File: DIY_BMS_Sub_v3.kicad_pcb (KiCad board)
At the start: 4 copper layers, 82 x 100 mm, 109 parts, among them J1 Conn_02x05_Top_Bottom, J2 Conn_02x05_Top_Bottom, J3 Conn_02x04_Top_Bottom, J4 Conn_02x04_Top_Bottom, J5 RJ45, Q1 Q_NMOS_GSD, Q2 Q_NMOS_GSD, Q3 Q_NMOS_GSD, Q4 Q_NMOS_GSD, Q5 Q_NMOS_GSD, Q6 Q_NMOS_GSD, SW1 SW_DIP_x04, U1 BQ76PL536A

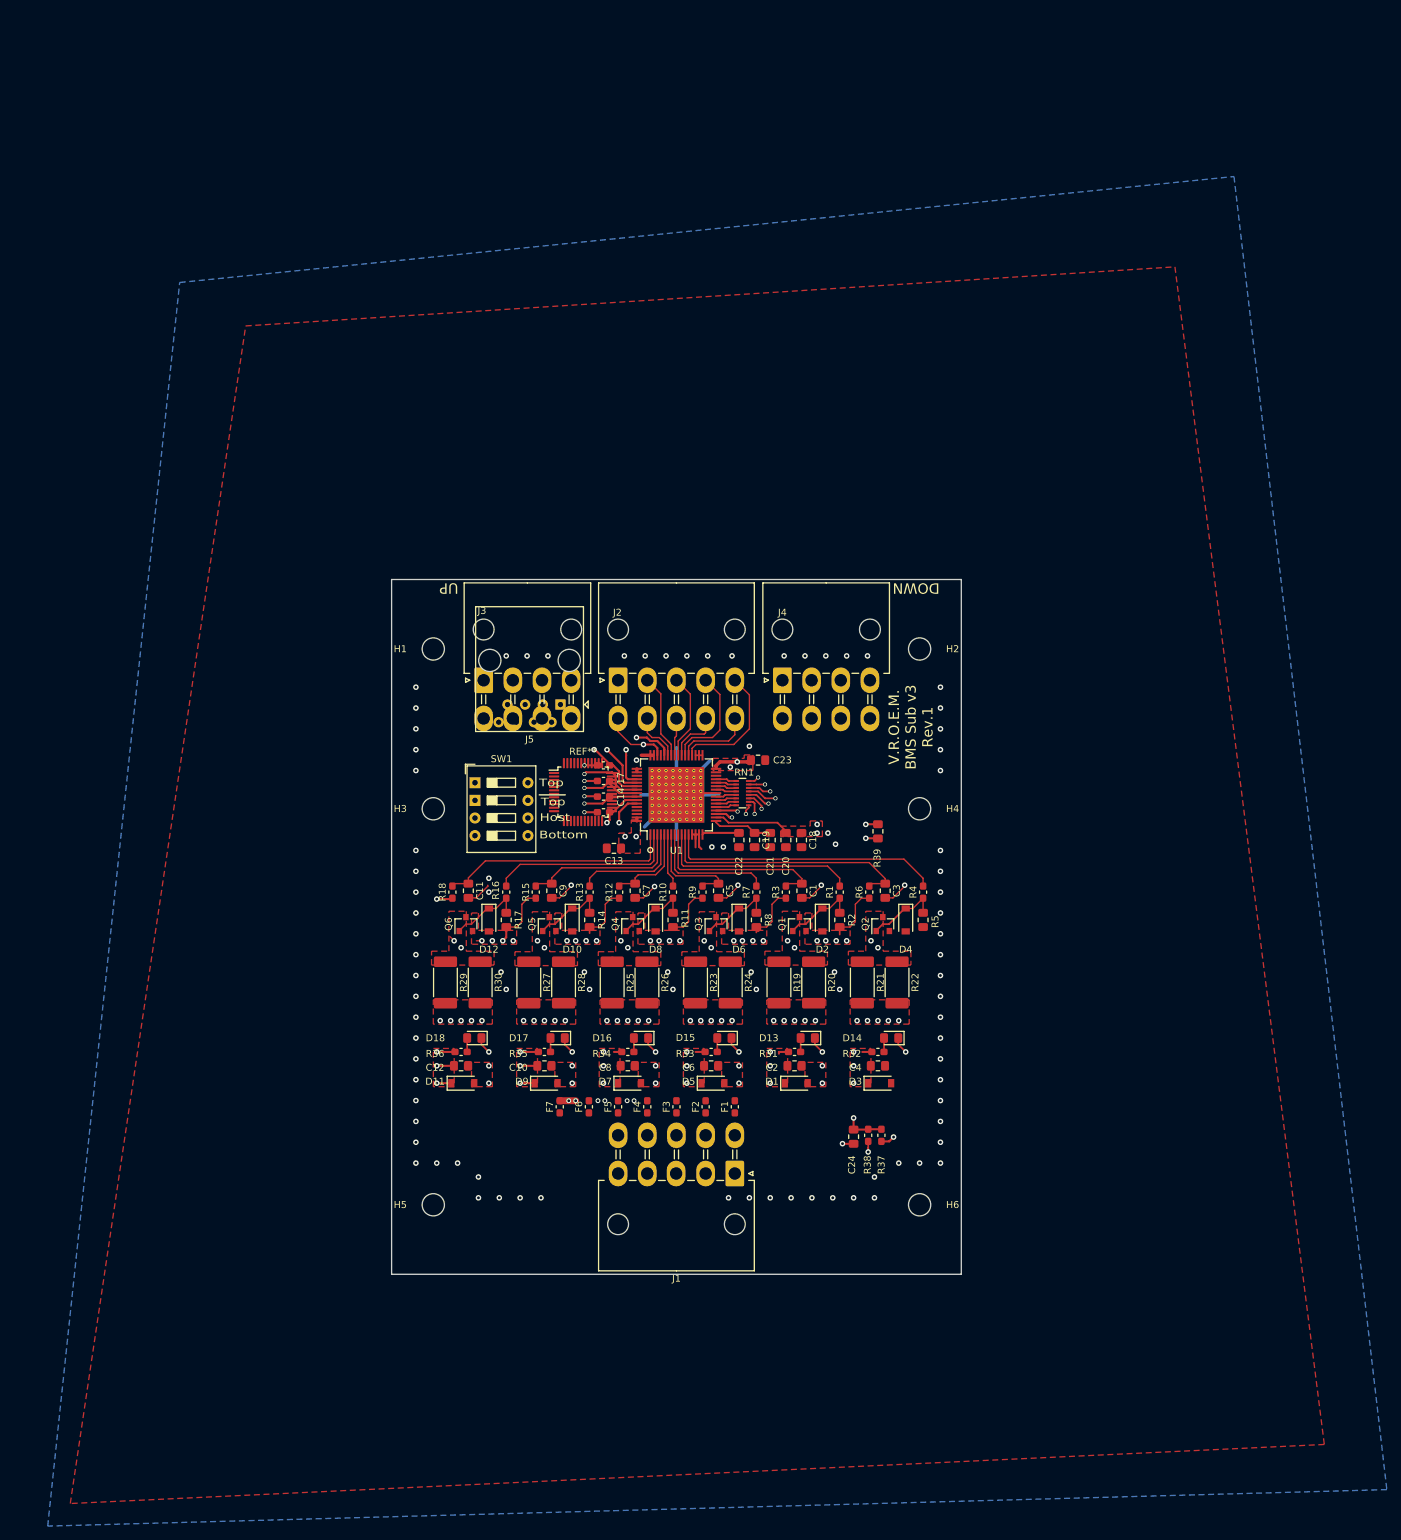
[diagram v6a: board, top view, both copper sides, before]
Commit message: Add files via upload
Changed board dimensions. Replaced Molex connectors from MiniFit to the smaller MicroFit-type.
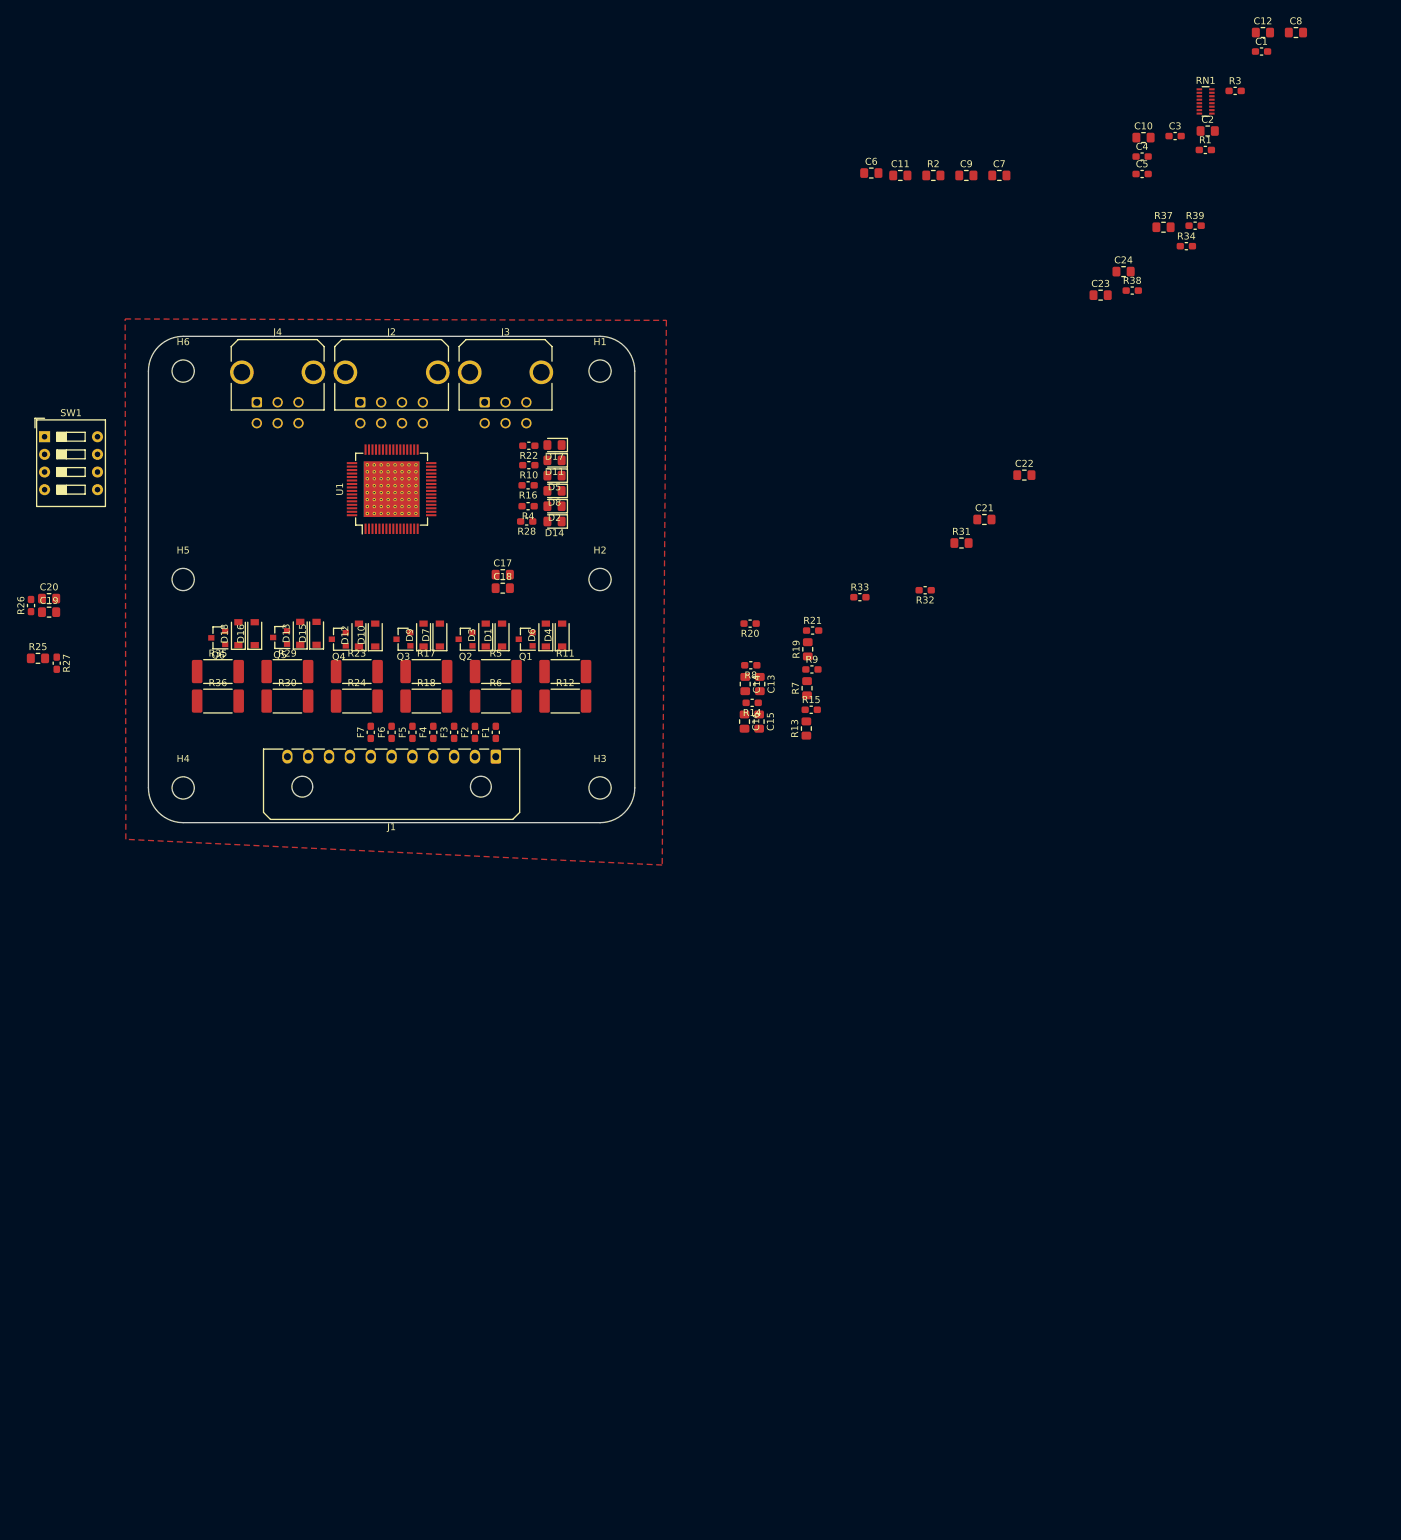
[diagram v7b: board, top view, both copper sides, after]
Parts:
- removed J5: RJ45, Connector_RJ:RJ45_Amphenol_54602-x08_Horizontal
- removed REF**: LQFP-48_7x7mm_P0.5mm, Package_QFP:LQFP-48_7x7mm_P0.5mm
- C1, C3, C4, C5: value 0.1u -> 33p; footprint Capacitor_SMD:C_0805_2012Metric_Pad1.15x1.40mm_HandSolder -> Capacitor_SMD:C_0603_1608Metric_Pad1.05x0.95mm_HandSolder
- C11, C7, C9: value 0.1u -> 2.2u
- C14, C15, C16, C17: value 33p -> 0.1u; footprint Capacitor_SMD:C_0603_1608Metric_Pad1.05x0.95mm_HandSolder -> Capacitor_SMD:C_0805_2012Metric_Pad1.15x1.40mm_HandSolder
- C20, C21, C23: value 2.2u -> 0.1u
- C22: value 10u -> 0.1u
- C24: value 47p -> 0.1u
- C6: value 0.1u -> 10u
- C8: value 0.1u -> 47p
- D11, D2, D5, D8: value 5V6 -> LED; footprint Diode_SMD:D_SOD-123 -> LED_SMD:LED_0805_2012Metric_Pad1.15x1.40mm_HandSolder
- D13, D15, D16, D18: value LED -> 5V6; footprint LED_SMD:LED_0805_2012Metric_Pad1.15x1.40mm_HandSolder -> Diode_SMD:D_SOD-123
- J1: value Conn_02x05_Top_Bottom -> Conn_01x11; footprint #_Connectors:Molex_Mini-Fit_Jr_5569-10A2_2x05_P4.20mm_Horizontal_with3d -> Connector_Molex:Molex_Micro-Fit_3.0_43650-1100_1x11_P3.00mm_Horizontal
- J2: value Conn_02x05_Top_Bottom -> Conn_02x04_Top_Bottom; footprint #_Connectors:Molex_Mini-Fit_Jr_5569-10A2_2x05_P4.20mm_Horizontal_with3d -> Connector_Molex:Molex_Micro-Fit_3.0_43045-0821_2x04-1MP_P3.00mm_Horizontal
- J3, J4: value Conn_02x04_Top_Bottom -> Conn_02x03_Top_Bottom; footprint #_Connectors:Molex_Mini-Fit_Jr_5569-08A2_2x04_P4.20mm_Horizontal_with3D -> Connector_Molex:Molex_Micro-Fit_3.0_43045-0621_2x03-1MP_P3.00mm_Horizontal
- R1: value 1K -> 1K82
- R10, R16, R4: value 1K -> 1k
- R11, R17, R5: value 1M -> 51; footprint Resistor_SMD:R_0805_2012Metric_Pad1.15x1.40mm_HandSolder -> Resistor_SMD:R_2512_6332Metric_Pad1.52x3.35mm_HandSolder
- R12, R18, R6: value 1K -> 51; footprint Resistor_SMD:R_0603_1608Metric_Pad1.05x0.95mm_HandSolder -> Resistor_SMD:R_2512_6332Metric_Pad1.52x3.35mm_HandSolder
- R13, R7: value 1K -> 1M; footprint Resistor_SMD:R_0603_1608Metric_Pad1.05x0.95mm_HandSolder -> Resistor_SMD:R_0805_2012Metric_Pad1.15x1.40mm_HandSolder
- R14, R8: value 1M -> 1K; footprint Resistor_SMD:R_0805_2012Metric_Pad1.15x1.40mm_HandSolder -> Resistor_SMD:R_0603_1608Metric_Pad1.05x0.95mm_HandSolder
- R19, R25: value 51 -> 1M; footprint Resistor_SMD:R_2512_6332Metric_Pad1.52x3.35mm_HandSolder -> Resistor_SMD:R_0805_2012Metric_Pad1.15x1.40mm_HandSolder
- R2: value 1M -> 100K
- R20, R21, R26, R27: value 51 -> 1K; footprint Resistor_SMD:R_2512_6332Metric_Pad1.52x3.35mm_HandSolder -> Resistor_SMD:R_0603_1608Metric_Pad1.05x0.95mm_HandSolder
- R22, R28: value 51 -> 1k; footprint Resistor_SMD:R_2512_6332Metric_Pad1.52x3.35mm_HandSolder -> Resistor_SMD:R_0603_1608Metric_Pad1.05x0.95mm_HandSolder
- R3: value 1K -> 1K47
- R31: value 1k -> 1M; footprint Resistor_SMD:R_0603_1608Metric_Pad1.05x0.95mm_HandSolder -> Resistor_SMD:R_0805_2012Metric_Pad1.15x1.40mm_HandSolder
- R32, R33: value 1k -> 1K
- R35, R36: value 1k -> 51; footprint Resistor_SMD:R_0603_1608Metric_Pad1.05x0.95mm_HandSolder -> Resistor_SMD:R_2512_6332Metric_Pad1.52x3.35mm_HandSolder
- R37: value 1K47 -> 1M; footprint Resistor_SMD:R_0603_1608Metric_Pad1.05x0.95mm_HandSolder -> Resistor_SMD:R_0805_2012Metric_Pad1.15x1.40mm_HandSolder
- R38: value 1K82 -> 1K
- R39: value 100K -> 1K; footprint Resistor_SMD:R_0805_2012Metric_Pad1.15x1.40mm_HandSolder -> Resistor_SMD:R_0603_1608Metric_Pad1.05x0.95mm_HandSolder
- moved C12 188.3 mm to (125.4, -78.7)
- moved C8 177.1 mm to (130.2, -78.7)
- moved H6 160.1 mm to (-30.0, -30.0)
- moved C10 159.0 mm to (108.2, -63.6)
- moved C2 147.1 mm to (117.5, -64.6)
- moved R34 141.1 mm to (114.4, -48.0), turned to 0 degrees
- moved C1 137.7 mm to (125.2, -76.0), turned to 0 degrees
- moved R37 136.9 mm to (111.1, -50.7), turned to 0 degrees
- moved C4 136.3 mm to (108.0, -60.9)
- moved R3 132.2 mm to (121.4, -70.3), turned to 0 degrees
- moved C6 130.6 mm to (69.0, -58.5)
- moved C24 130.4 mm to (105.4, -44.3), turned to 0 degrees
- moved R38 127.4 mm to (106.6, -41.6), turned to 0 degrees
- moved C11 120.3 mm to (73.2, -58.2), turned to 0 degrees
- moved C5 119.8 mm to (108.0, -58.4), turned to 0 degrees
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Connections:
- C1 pad 1: /S2_components/VC+ -> SW_NotTop
- C1 pad 2: AGND -> SDO_N
- C10 pad 1: /C5 -> Net-(C10-Pad1)
- C10 pad 2: /C4 -> AGND
- C11 pad 1: /S6_components/VC+ -> AGND
- C11 pad 2: AGND -> LDOD
- C12 pad 1: /C6 -> LDOD
- C12 pad 2: /C5 -> AGND
- C13 pad 1: AGND -> /C2
- C13 pad 2: /C6 -> /C1
- C14 pad 1: SW_NotTop -> /S2_components/VC+
- C14 pad 2: DRDY_N -> AGND
- C15 pad 1: SW_NotTop -> /C1
- C15 pad 2: ALERT_N -> AGND
- C16 pad 1: SW_NotTop -> /S1_components/VC+
- C16 pad 2: FAULT_N -> AGND
- C17 pad 1: SW_NotTop -> S3
- C17 pad 2: SDO_N -> /C2
- C18 pad 1: LDOD -> /S3_components/VC+
- C19 pad 1: Net-(C19-Pad1) -> /C4
- C19 pad 2: AGND -> S3
- C2 pad 1: /C2 -> AGND
- C2 pad 2: /C1 -> /C6
- C20 pad 1: AGND -> /S4_components/VC+
- C20 pad 2: LDOD -> AGND
- C21 pad 1: AGND -> /C5
- C21 pad 2: Net-(C19-Pad1) -> /C4
- C22 pad 1: AGND -> /S5_components/VC+
- C22 pad 2: Net-(C22-Pad2) -> AGND
- C23 pad 1: 5VDC -> /C6
- C23 pad 2: AGND -> /C5
- C24 pad 1: Net-(C24-Pad1) -> /S6_components/VC+
- C24 pad 2: 5VDC -> AGND
- C3 pad 1: /S1_components/VC+ -> SW_NotTop
- C3 pad 2: AGND -> FAULT_N
- C4 pad 1: /C1 -> SW_NotTop
- C4 pad 2: AGND -> ALERT_N
- C5 pad 1: /S3_components/VC+ -> SW_NotTop
- C5 pad 2: AGND -> DRDY_N
- C6 pad 1: S3 -> AGND
- C6 pad 2: /C2 -> Net-(C6-Pad2)
- C7 pad 1: /S4_components/VC+ -> 5VDC
- C8 pad 1: /C4 -> Net-(C8-Pad1)
- C8 pad 2: S3 -> 5VDC
- C9 pad 1: /S5_components/VC+ -> AGND
- C9 pad 2: AGND -> Net-(C10-Pad1)
- D10 pad 1: Net-(D10-Pad1) -> /C4
- D10 pad 2: /C4 -> S3
- D11 pad 1: /C6 -> Net-(D11-Pad1)
- D11 pad 2: /C5 -> Net-(D11-Pad2)
- D12 pad 2: /C5 -> S3
- D13 pad 1: Net-(D13-Pad1) -> /C5
- D13 pad 2: Net-(D13-Pad2) -> /C4
- D15 pad 2: Net-(D15-Pad2) -> /C4
- D16 pad 1: Net-(D16-Pad1) -> /C6
- D16 pad 2: Net-(D16-Pad2) -> /C5
- D18 pad 2: Net-(D18-Pad2) -> /C5
- D2 pad 2: /C1 -> Net-(D2-Pad2)
- D3 pad 1: /C1 -> Net-(D3-Pad1)
- D3 pad 2: AGND -> /C1
- D4 pad 1: Net-(D4-Pad1) -> /C1
- D5 pad 1: S3 -> Net-(D5-Pad1)
- D5 pad 2: /C2 -> Net-(D5-Pad2)
- D6 pad 2: /C2 -> AGND
- D7 pad 1: /C4 -> S3
- D7 pad 2: S3 -> /C2
- D8 pad 2: S3 -> Net-(D8-Pad2)
- D9 pad 1: /C5 -> Net-(D9-Pad1)
- D9 pad 2: /C4 -> /C2
- F4 pad 1: C3 -> (no net)
- J1 pad 1: 5VDC -> S0
- J1 pad 10: S4 -> (no net)
- J1 pad 2: Temp- -> S1
- J1 pad 3: (no net) -> S2
- J1 pad 4: S6 -> S3
- J1 pad 5: S5 -> S4
- J1 pad 6: S0 -> S5
- J1 pad 7: S1 -> S6
- J1 pad 8: S2 -> (no net)
- J1 pad 9: C3 -> (no net)
- J2 pad 1: AGND -> (no net)
- J2 pad 2: SDI_H -> (no net)
- J2 pad 3: SCLK_H -> (no net)
- J2 pad 4: ALERT_H -> (no net)
- J2 pad 5: CONV_H -> (no net)
- J2 pad 6: LDOD -> (no net)
- J2 pad 7: CS_H -> (no net)
- J2 pad 8: SDO_H -> (no net)
- J3 pad 2: FAULT_N -> SDO_N
- J3 pad 3: SDO_N -> CS_N
- J3 pad 4: CS_N -> CONV_N
- J3 pad 5: CONV_N -> SCLK_N
- J3 pad 6: ALERT_N -> SDI_N
- J4 pad 1: SDI_S -> DRDY_S
- J4 pad 2: SCLK_S -> (no net)
- J4 pad 3: ALERT_S -> CS_S
- J4 pad 5: CS_S -> SCLK_S
- J4 pad 6: SDO_S -> (no net)
- Q1 pad 1: Net-(D2-Pad1) -> Net-(D6-Pad1)
- Q1 pad 2: /C1 -> AGND
- Q1 pad 3: Net-(D13-Pad1) -> Net-(D5-Pad1)
- Q2 pad 1: Net-(D4-Pad1) -> Net-(D3-Pad1)
- Q2 pad 2: AGND -> /C1
- Q2 pad 3: Net-(D14-Pad1) -> Net-(D2-Pad1)
- Q3 pad 1: Net-(D6-Pad1) -> Net-(D9-Pad1)
- Q3 pad 3: Net-(D15-Pad1) -> Net-(D8-Pad1)
- Q4 pad 1: Net-(D8-Pad1) -> Net-(D12-Pad1)
- Q4 pad 3: Net-(D16-Pad1) -> Net-(D11-Pad1)
- Q5 pad 1: Net-(D10-Pad1) -> Net-(D15-Pad1)
- Q5 pad 3: Net-(D17-Pad1) -> Net-(D14-Pad1)
- Q6 pad 1: Net-(D12-Pad1) -> Net-(D18-Pad1)
- Q6 pad 3: Net-(D18-Pad1) -> Net-(D17-Pad1)
- R1 pad 1: Net-(D2-Pad1) -> Net-(R1-Pad1)
- R1 pad 2: /S2_components/Balancing -> Net-(C8-Pad1)
- R10 pad 1: Net-(D8-Pad1) -> Net-(D5-Pad2)
- R10 pad 2: /S4_components/Balancing -> /C1
- R11 pad 1: S3 -> Net-(D5-Pad1)
- R11 pad 2: Net-(D8-Pad1) -> /C1
- R12 pad 1: /C4 -> Net-(D5-Pad1)
- R12 pad 2: /S4_components/VC+ -> /C1
- R13 pad 1: Net-(D10-Pad1) -> AGND
- R13 pad 2: /S5_components/Balancing -> Net-(D6-Pad1)
- R14 pad 1: /C4 -> /C1
- R14 pad 2: Net-(D10-Pad1) -> /S1_components/VC+
- R15 pad 1: /C5 -> Net-(D6-Pad1)
- R15 pad 2: /S5_components/VC+ -> /S1_components/Balancing
- R16 pad 1: Net-(D12-Pad1) -> Net-(D8-Pad2)
- R16 pad 2: /S6_components/Balancing -> S3
- R17 pad 1: /C5 -> Net-(D8-Pad1)
- R17 pad 2: Net-(D12-Pad1) -> S3
- R18 pad 1: /C6 -> Net-(D8-Pad1)
- R18 pad 2: /S6_components/VC+ -> S3
- R19 pad 1: Net-(D13-Pad1) -> /C2
- R19 pad 2: /C2 -> Net-(D9-Pad1)
- R2 pad 1: /C1 -> 5VDC
- R2 pad 2: Net-(D2-Pad1) -> SW_Host
- R20 pad 1: Net-(D13-Pad1) -> S3
- R20 pad 2: /C2 -> /S3_components/VC+
- R21 pad 1: Net-(D14-Pad1) -> Net-(D9-Pad1)
- R21 pad 2: /C1 -> /S3_components/Balancing
- R22 pad 1: Net-(D14-Pad1) -> Net-(D11-Pad2)
- R22 pad 2: /C1 -> /C4
- R23 pad 1: Net-(D15-Pad1) -> Net-(D11-Pad1)
- R23 pad 2: S3 -> /C4
- R24 pad 1: Net-(D15-Pad1) -> Net-(D11-Pad1)
- R24 pad 2: S3 -> /C4
- R25 pad 1: Net-(D16-Pad1) -> S3
- R25 pad 2: /C4 -> Net-(D12-Pad1)
- R26 pad 1: Net-(D16-Pad1) -> /C4
- R26 pad 2: /C4 -> /S4_components/VC+
- R27 pad 1: Net-(D17-Pad1) -> Net-(D12-Pad1)
- R27 pad 2: /C5 -> /S4_components/Balancing
- R28 pad 1: Net-(D17-Pad1) -> Net-(D14-Pad2)
- R29 pad 1: Net-(D18-Pad1) -> Net-(D14-Pad1)
- R29 pad 2: /C6 -> /C5
- R3 pad 1: /C2 -> Net-(C8-Pad1)
- R3 pad 2: /S2_components/VC+ -> (no net)
- R30 pad 1: Net-(D18-Pad1) -> Net-(D14-Pad1)
- R30 pad 2: /C6 -> /C5
- R31 pad 1: Net-(D13-Pad2) -> /C4
- R31 pad 2: /C2 -> Net-(D15-Pad1)
- R32 pad 1: Net-(D14-Pad2) -> /C5
- R32 pad 2: /C1 -> /S5_components/VC+
- R33 pad 1: Net-(D15-Pad2) -> Net-(D15-Pad1)
- R33 pad 2: S3 -> /S5_components/Balancing
- R34 pad 1: Net-(D16-Pad2) -> Net-(D17-Pad2)
- R34 pad 2: /C4 -> /C6
- R35 pad 1: Net-(D17-Pad2) -> Net-(D17-Pad1)
- R35 pad 2: /C5 -> /C6
- R36 pad 1: Net-(D18-Pad2) -> Net-(D17-Pad1)
- R37 pad 1: Net-(C24-Pad1) -> /C5
- R37 pad 2: Temp- -> Net-(D18-Pad1)
- R38 pad 1: Net-(R38-Pad1) -> /C6
- R38 pad 2: Net-(C24-Pad1) -> /S6_components/VC+
- R39 pad 1: 5VDC -> Net-(D18-Pad1)
- R39 pad 2: SW_Host -> /S6_components/Balancing
- R4 pad 1: Net-(D4-Pad1) -> Net-(D2-Pad2)
- R4 pad 2: /S1_components/Balancing -> /C2
- R5 pad 1: AGND -> Net-(D2-Pad1)
- R5 pad 2: Net-(D4-Pad1) -> /C2
- R6 pad 1: /C1 -> Net-(D2-Pad1)
- R6 pad 2: /S1_components/VC+ -> /C2
- R7 pad 1: Net-(D6-Pad1) -> /C1
- R7 pad 2: /S3_components/Balancing -> Net-(D3-Pad1)
- R8 pad 2: Net-(D6-Pad1) -> /S2_components/VC+
- R9 pad 1: S3 -> Net-(D3-Pad1)
- R9 pad 2: /S3_components/VC+ -> /S2_components/Balancing
- RN1 pad 3: ALERT_S -> (no net)
- RN1 pad 4: FAULT_S -> (no net)
- RN1 pad 6: SDO_S -> (no net)
- RN1 pad 7: SDI_S -> (no net)
- U1 pad 16: Net-(C22-Pad2) -> Net-(C6-Pad2)
- U1 pad 17: Net-(C19-Pad1) -> Net-(C10-Pad1)
- U1 pad 19: Net-(R38-Pad1) -> Net-(R1-Pad1)
- U1 pad 20: Net-(C24-Pad1) -> Net-(C8-Pad1)
- U1 pad 36: CONV_H -> (no net)
- U1 pad 37: DRDY_H -> (no net)
- U1 pad 38: ALERT_H -> (no net)
- U1 pad 39: FAULT_H -> (no net)
- U1 pad 40: SCLK_H -> (no net)
- U1 pad 41: SDO_H -> (no net)
- U1 pad 42: SDI_H -> (no net)
- U1 pad 43: CS_H -> (no net)
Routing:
- net S6: track 102.6 -> 0.00 mm, vias 11 -> 0
- net 5VDC: track 99.1 -> 0.00 mm, vias 4 -> 0
- net Net-(C24-Pad1): track 86.4 -> 0.00 mm, vias 3 -> 0
- net Net-(R38-Pad1): track 85.5 -> 0.00 mm, vias 3 -> 0
- net CONV_S: track 79.1 -> 0.00 mm, vias 1 -> 0
- net AGND: track 74.0 -> 0.00 mm, vias 95 -> 0
- net SW_Host: track 73.2 -> 0.00 mm, vias 2 -> 0
- net /C5: track 60.8 -> 0.00 mm, vias 14 -> 0
- net LDOD: track 58.6 -> 0.00 mm, vias 3 -> 0
- net S3: track 53.2 -> 0.00 mm, vias 14 -> 0
- net S1: track 48.7 -> 0.00 mm, vias 14 -> 0
- net S2: track 47.2 -> 0.00 mm, vias 14 -> 0
- net S4: track 46.2 -> 0.00 mm, vias 14 -> 0
- net SW_NotTop: track 42.8 -> 0.00 mm, vias 4 -> 0
- net /S1_components/Balancing: track 39.4 -> 0.00 mm
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- removed copper zone on F.Cu, net /C5
- removed copper zone on F.Cu, net 5VDC
- removed copper zone on B.Cu, net AGND
- removed copper zone on F.Cu, net LDOD
- removed copper zone on F.Cu, net Net-(D13-Pad1)
- removed copper zone on F.Cu, net Net-(D14-Pad1)
- removed copper zone on F.Cu, net Net-(D15-Pad1)
- removed copper zone on F.Cu, net Net-(D16-Pad1)
- removed copper zone on F.Cu, net Net-(D17-Pad1)
- removed copper zone on F.Cu, net Net-(D18-Pad1)
- removed copper zone on F.Cu, net S1
- removed copper zone on F.Cu, net S2
- removed copper zone on F.Cu, net S3
- removed copper zone on F.Cu, net S4
- removed copper zone on F.Cu, net S5
- removed copper zone on F.Cu, net S6
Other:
- board size 82 x 100 mm -> 70 x 70 mm
- board text removed: "Bottom"
- board text removed: "C14-17"
- board text removed: "DOWN"
- board text removed: "Host"
- board text removed: "JLCJLCJLCJLC"
- board text removed: "Top"
- board text removed: "UP"
- board text removed: "V.R.O.E.M. BMS Sub v3 Rev.1"

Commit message: Add files via upload
Placed most components. Started routing and placing vias.
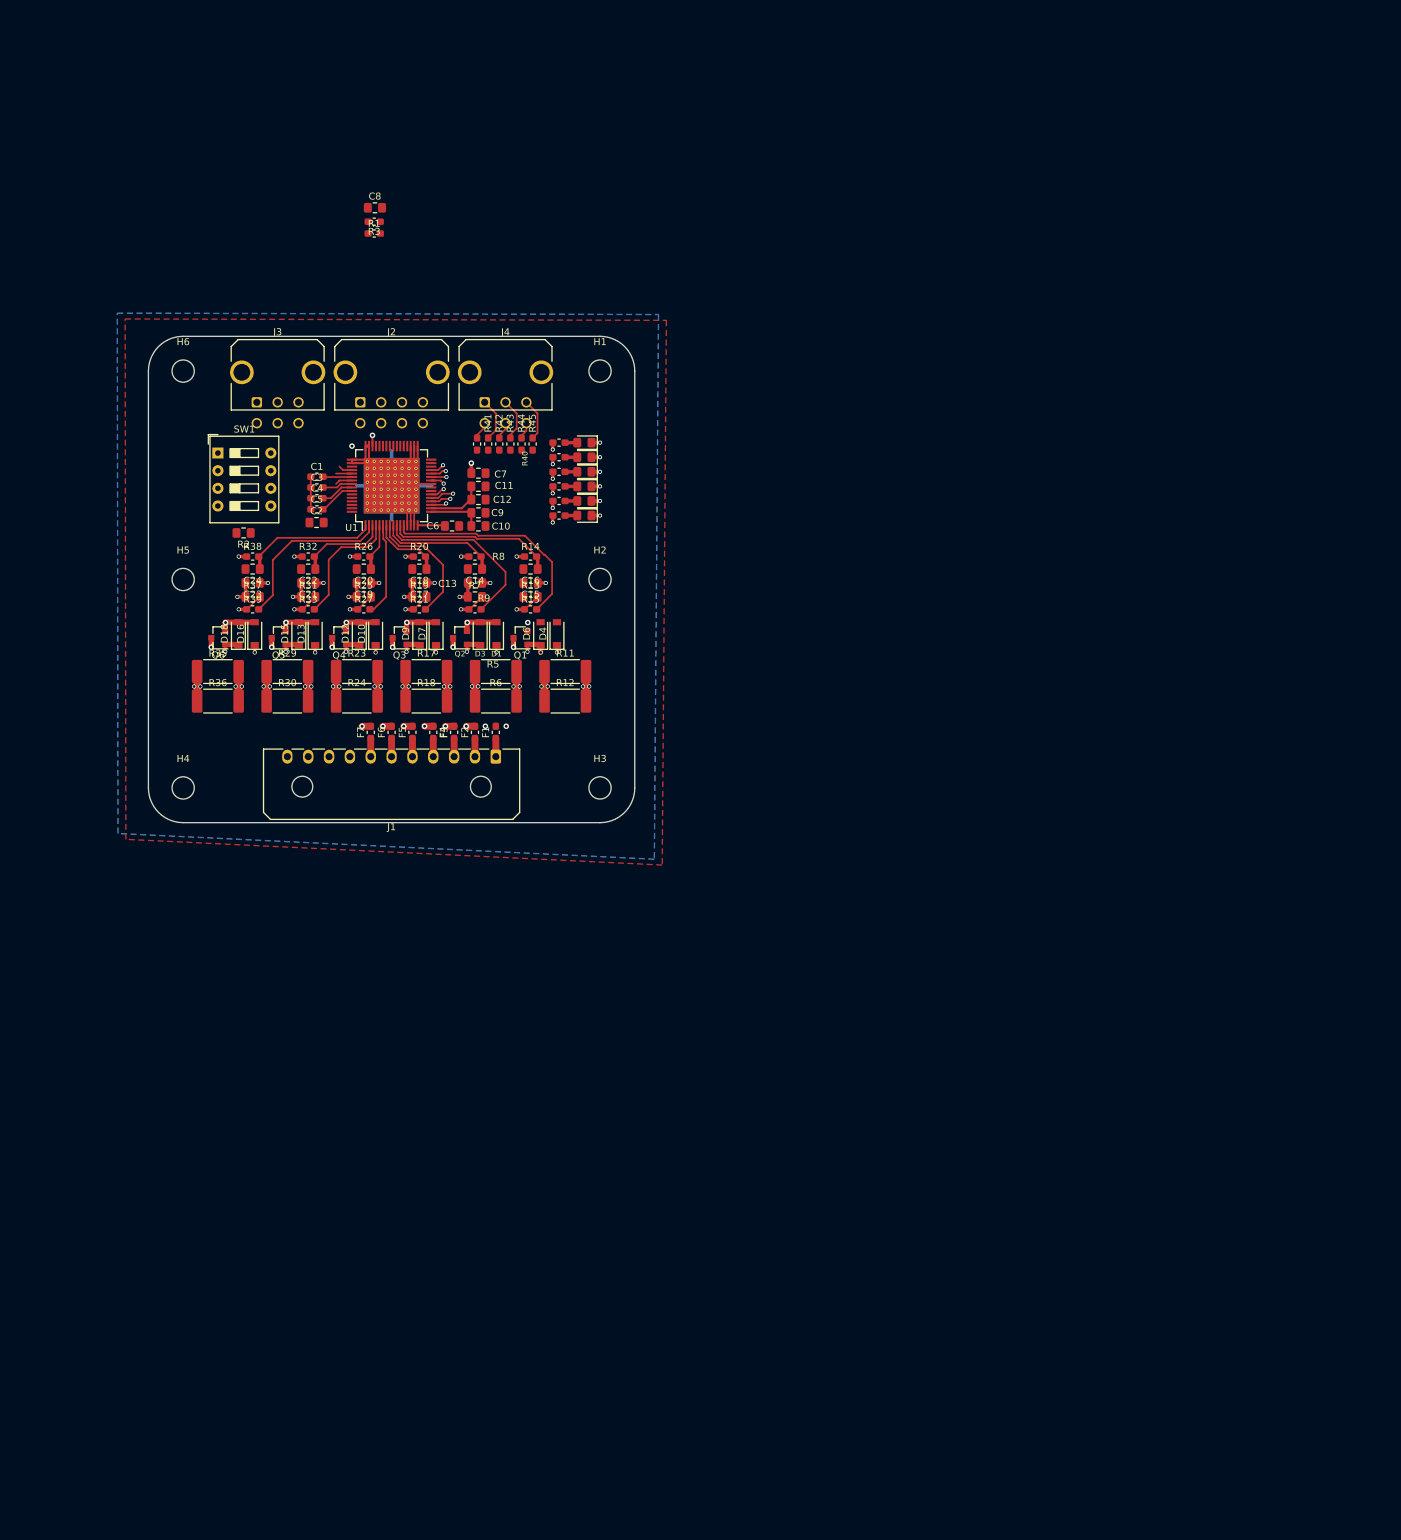
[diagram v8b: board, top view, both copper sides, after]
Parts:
- removed RN1: 1K_Pack08, Resistor_SMD:R_Array_Convex_8x0602
- added R40: 1k, Resistor_SMD:R_0603_1608Metric_Pad1.05x0.95mm_HandSolder, F.Cu at (12.3, -19.5)
- added R41: 1k, Resistor_SMD:R_0603_1608Metric_Pad1.05x0.95mm_HandSolder, F.Cu at (13.9, -19.5)
- added R42: 1k, Resistor_SMD:R_0603_1608Metric_Pad1.05x0.95mm_HandSolder, F.Cu at (15.5, -19.5)
- added R43: 1k, Resistor_SMD:R_0603_1608Metric_Pad1.05x0.95mm_HandSolder, F.Cu at (17.1, -19.5)
- added R44: 1k, Resistor_SMD:R_0603_1608Metric_Pad1.05x0.95mm_HandSolder, F.Cu at (18.7, -19.5)
- added R45: 1k, Resistor_SMD:R_0603_1608Metric_Pad1.05x0.95mm_HandSolder, F.Cu at (20.3, -19.5)
- moved C1 149.1 mm to (-10.8, -14.8)
- moved R39 146.5 mm to (-20.0, 4.30)
- moved R37 141.5 mm to (-20.0, 2.50)
- moved C2 140.1 mm to (-10.8, -8.20)
- moved C8 134.9 mm to (-2.40, -53.5)
- moved C3 133.5 mm to (-10.8, -13.2)
- moved C24 132.5 mm to (-20.0, -1.50), turned to 180 degrees
- moved R38 132.3 mm to (-20.0, -3.30)
- moved C12 131.4 mm to (12.5, -11.5)
- moved C23 128.9 mm to (-20.0, 0.50), turned to 180 degrees
- moved C4 128.6 mm to (-10.8, -11.7)
- moved C5 128.2 mm to (-10.8, -10.1)
- moved R3 125.3 mm to (-2.50, -51.5), turned to 180 degrees
- moved R1 120.2 mm to (-2.50, -49.8)
- moved R2 111.8 mm to (-21.3, -6.70), turned to 180 degrees
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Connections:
- C17 pad 1: S3 -> /C3
- C19 pad 2: S3 -> /C3
- D10 pad 2: S3 -> /C3
- D12 pad 2: S3 -> /C3
- D7 pad 1: S3 -> /C3
- F4 pad 1: (no net) -> S3
- F4 pad 2: S3 -> /C3
- J4 pad 2: (no net) -> SDO_S
- J4 pad 6: (no net) -> SDI_S
- Q4 pad 2: S3 -> /C3
- R16 pad 2: S3 -> /C3
- R17 pad 2: S3 -> /C3
- R18 pad 2: S3 -> /C3
- R20 pad 1: S3 -> /C3
- R25 pad 1: S3 -> /C3
- SW1 pad 1: S6 -> /C6
- SW1 pad 2: S6 -> /C6
- U1 pad 23: Net-(RN1-Pad14) -> (no net)
- U1 pad 24: Net-(RN1-Pad13) -> (no net)
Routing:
- net AGND: track 0.00 -> 83.0 mm, vias 0 -> 4
- net /C1: track 0.00 -> 59.8 mm, vias 0 -> 9
- net /C5: track 0.00 -> 55.2 mm, vias 0 -> 9
- net /C2: track 0.00 -> 51.2 mm, vias 0 -> 9
- net /C3: track 0.00 -> 45.2 mm, vias 0 -> 9
- net /C4: track 0.00 -> 45.1 mm, vias 0 -> 9
- net /S1_components/Balancing: track 0.00 -> 32.1 mm
- net /C6: track 0.00 -> 30.4 mm, vias 0 -> 7
- net /S2_components/Balancing: track 0.00 -> 26.3 mm
- net /S6_components/Balancing: track 0.00 -> 24.7 mm
- net /S1_components/VC+: track 0.00 -> 24.1 mm
- net /S6_components/VC+: track 0.00 -> 19.5 mm
- net Net-(D5-Pad1): track 0.00 -> 19.0 mm, vias 0 -> 4
- net /S3_components/Balancing: track 0.00 -> 18.6 mm
- net /S5_components/Balancing: track 0.00 -> 18.2 mm
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- added copper zone on B.Cu, net AGND
